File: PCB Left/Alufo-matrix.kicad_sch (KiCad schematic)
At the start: 59 parts, among them K11 PG1350, K12 PG1350, K13 PG1350, K14 PG1350, K15 PG1350, K16 PG1350, K21 PG1350, K22 PG1350, K23 PG1350, K24 PG1350, K25 PG1350, K26 PG1350, K31 PG1350, K32 PG1350, K33 PG1350, K34 PG1350, K35 PG1350, K36 PG1350_1½U

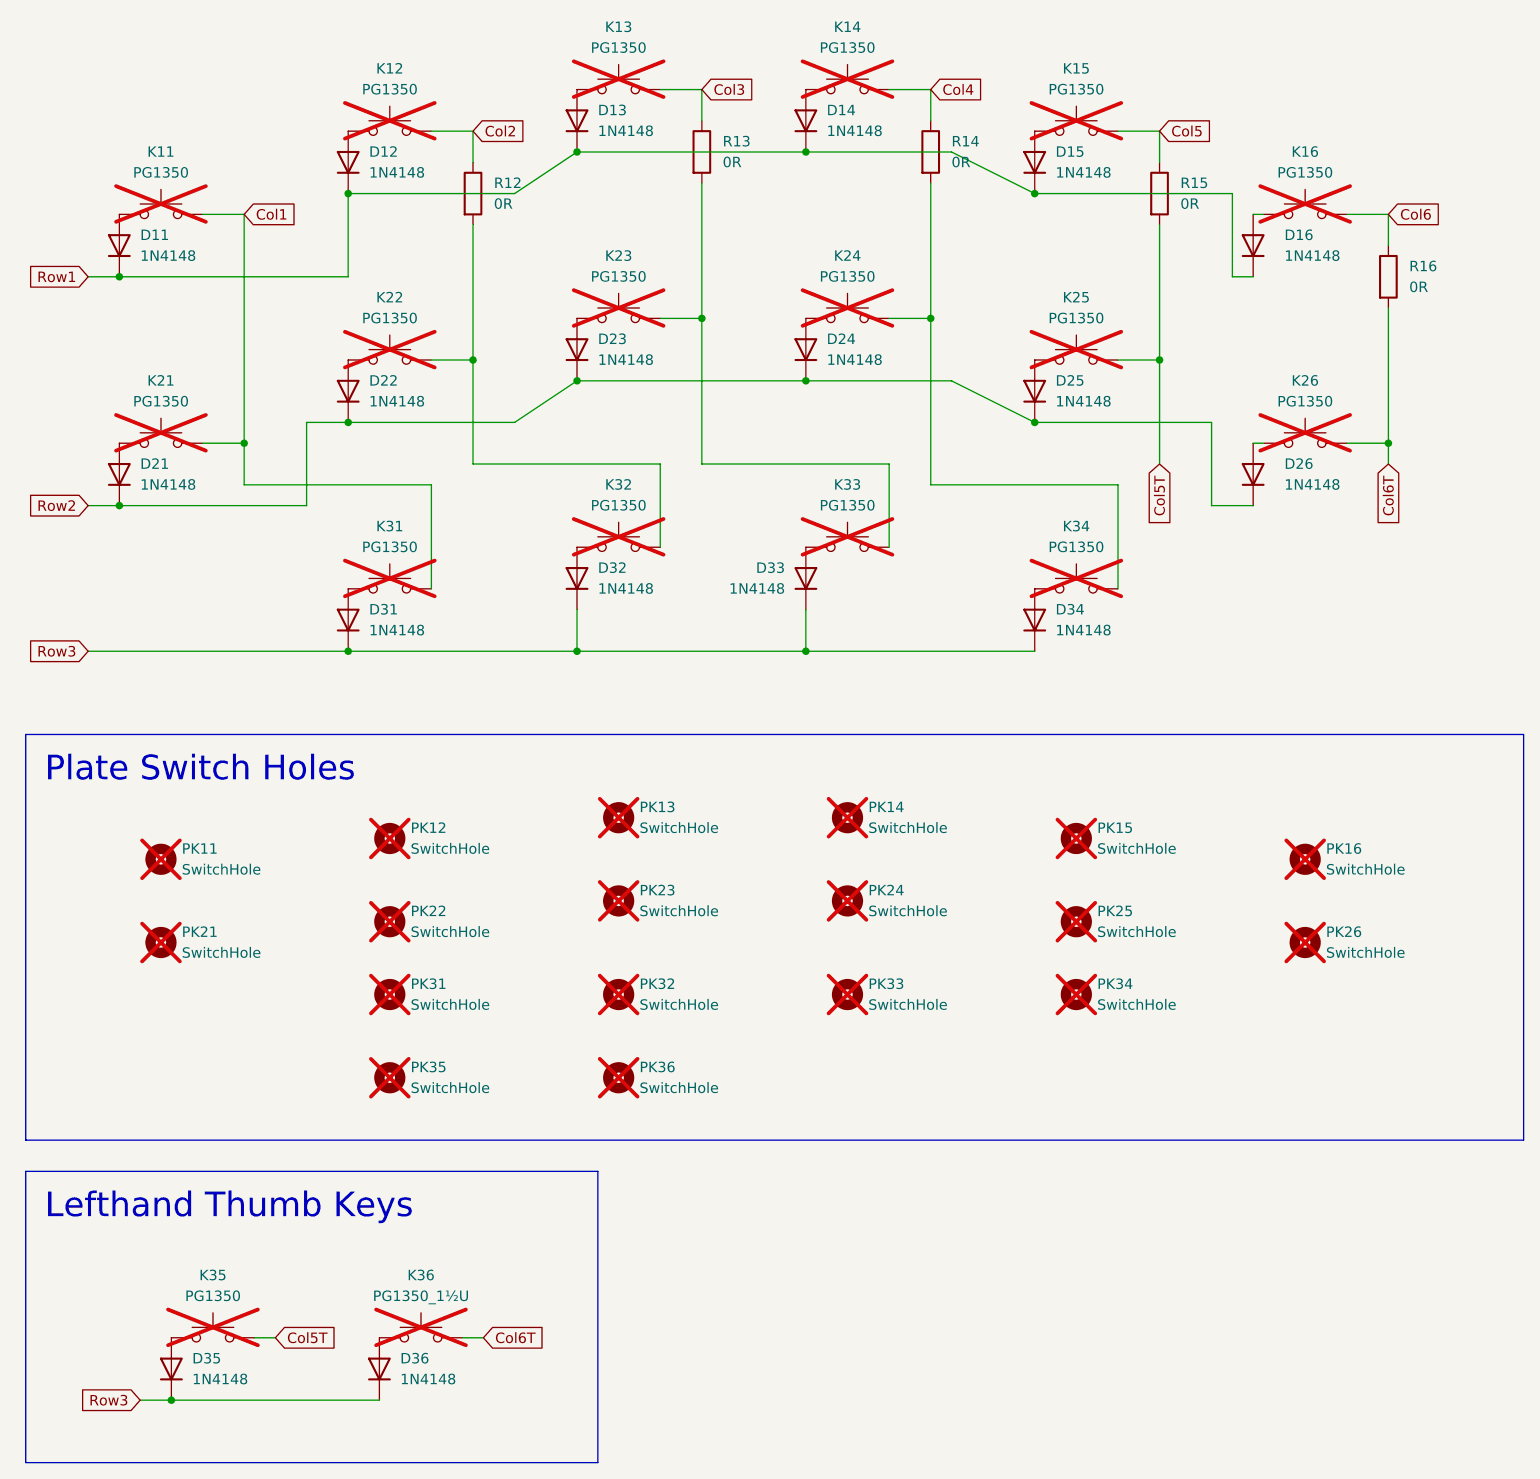
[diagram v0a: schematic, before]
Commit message: Unset DNP on all symbols
It causes the symbol to be obscured by a big red cross in the schematic!
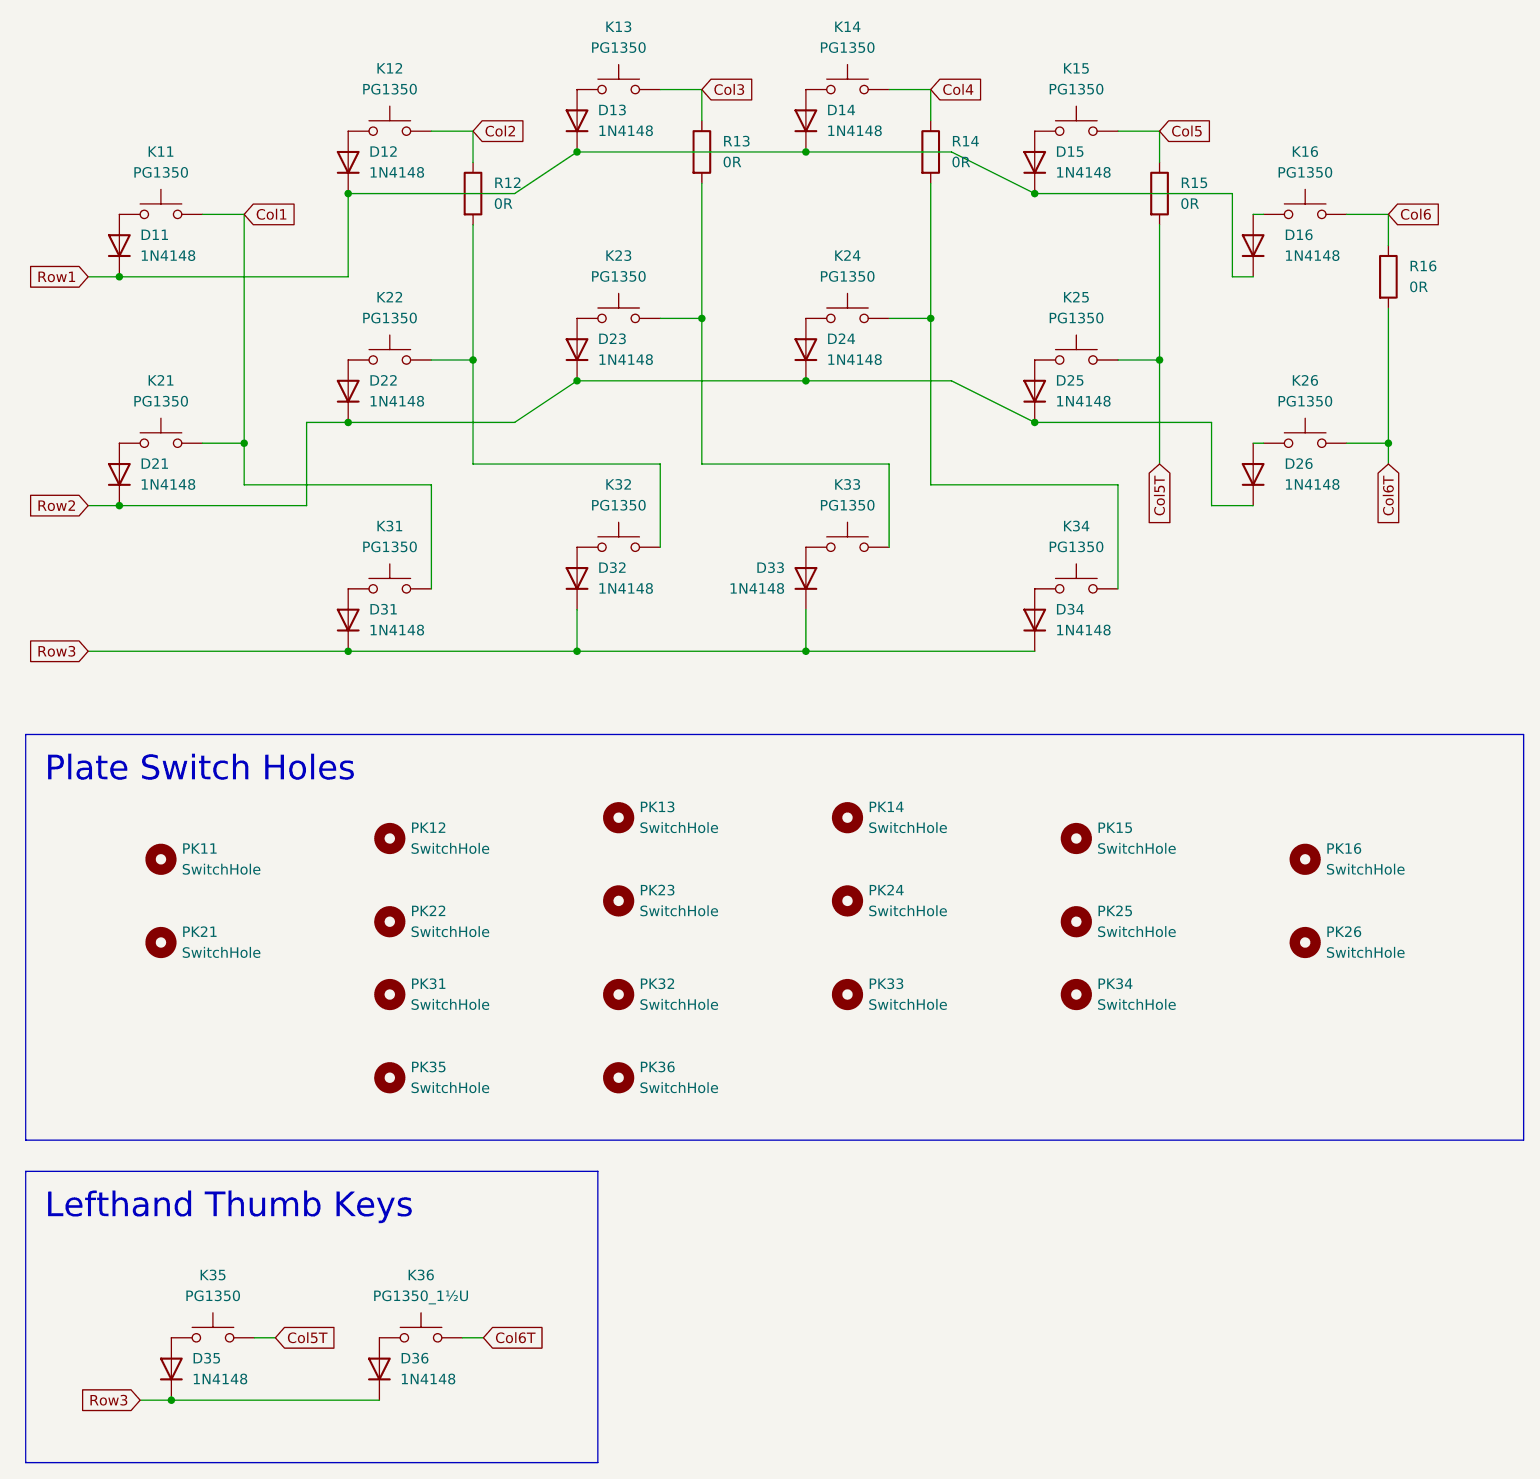
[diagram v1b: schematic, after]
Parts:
- K11, K12, K13, K14, K15, K16, K21, K22, K23, K24, K25, K26, K31, K32, K33, K34, K35, K36, PK11, PK12, PK13, PK14, PK15, PK16, PK21, PK22, PK23, PK24, PK25, PK26, PK31, PK32, PK33, PK34, PK35, PK36: now fitted
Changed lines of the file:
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@@
 		(in_bom no)
 		(on_board yes)
-		(dnp yes)
+		(dnp no)
 		(fields_autoplaced yes)
 		(property "Reference" "PK32"
@@
 		(in_bom no)
 		(on_board yes)
-		(dnp yes)
+		(dnp no)
 		(fields_autoplaced yes)
 		(property "Reference" "PK21"
@@
 		(in_bom yes)
 		(on_board yes)
-		(dnp yes)
+		(dnp no)
 		(property "Reference" "K24"
 			(at 161.29 48.26 0)
@@
 		(in_bom yes)
 		(on_board yes)
-		(dnp yes)
+		(dnp no)
 		(property "Reference" "K23"
 			(at 133.35 48.26 0)
@@
 		(in_bom no)
 		(on_board yes)
-		(dnp yes)
+		(dnp no)
 		(fields_autoplaced yes)
 		(property "Reference" "PK22"
@@
 		(in_bom yes)
 		(on_board yes)
-		(dnp yes)
+		(dnp no)
 		(property "Reference" "K33"
 			(at 161.29 76.2 0)
@@
 		(in_bom yes)
 		(on_board yes)
-		(dnp yes)
+		(dnp no)
 		(property "Reference" "K14"
 			(at 161.29 20.32 0)
@@
 		(in_bom yes)
 		(on_board yes)
-		(dnp yes)
+		(dnp no)
 		(property "Reference" "K34"
 			(at 189.23 81.28 0)
@@
 		(in_bom no)
 		(on_board yes)
-		(dnp yes)
+		(dnp no)
 		(fields_autoplaced yes)
 		(property "Reference" "PK15"
@@
 		(in_bom yes)
 		(on_board yes)
-		(dnp yes)
+		(dnp no)
 		(property "Reference" "K36"
 			(at 109.22 172.72 0)
@@
 		(in_bom yes)
 		(on_board yes)
-		(dnp yes)
+		(dnp no)
 		(property "Reference" "K11"
 			(at 77.47 35.56 0)
@@
 		(in_bom no)
 		(on_board yes)
-		(dnp yes)
+		(dnp no)
 		(fields_autoplaced yes)
 		(property "Reference" "PK14"
@@
 		(in_bom no)
 		(on_board yes)
-		(dnp yes)
+		(dnp no)
 		(fields_autoplaced yes)
 		(property "Reference" "PK13"
@@
 		(in_bom yes)
 		(on_board yes)
-		(dnp yes)
+		(dnp no)
 		(property "Reference" "K31"
 			(at 105.41 81.28 0)
@@
 		(in_bom yes)
 		(on_board yes)
-		(dnp yes)
+		(dnp no)
 		(property "Reference" "K21"
 			(at 77.47 63.5 0)
@@
 		(in_bom yes)
 		(on_board yes)
-		(dnp yes)
+		(dnp no)
 		(property "Reference" "K15"
 			(at 189.23 25.4 0)
@@
 		(in_bom yes)
 		(on_board yes)
-		(dnp yes)
+		(dnp no)
 		(property "Reference" "K32"
 			(at 133.35 76.2 0)
@@
 		(in_bom yes)
 		(on_board yes)
-		(dnp yes)
+		(dnp no)
 		(property "Reference" "K12"
 			(at 105.41 25.4 0)
@@
 		(in_bom yes)
 		(on_board yes)
-		(dnp yes)
+		(dnp no)
 		(property "Reference" "K35"
 			(at 83.82 172.72 0)
@@
 		(in_bom yes)
 		(on_board yes)
-		(dnp yes)
+		(dnp no)
 		(property "Reference" "K25"
 			(at 189.23 53.34 0)
@@
 		(in_bom no)
 		(on_board yes)
-		(dnp yes)
+		(dnp no)
 		(fields_autoplaced yes)
 		(property "Reference" "PK33"
@@
 		(in_bom no)
 		(on_board yes)
-		(dnp yes)
+		(dnp no)
 		(fields_autoplaced yes)
 		(property "Reference" "PK12"
@@
 		(in_bom no)
 		(on_board yes)
-		(dnp yes)
+		(dnp no)
 		(fields_autoplaced yes)
 		(property "Reference" "PK23"
@@
 		(in_bom no)
 		(on_board yes)
-		(dnp yes)
+		(dnp no)
 		(fields_autoplaced yes)
 		(property "Reference" "PK25"
@@
 		(in_bom no)
 		(on_board yes)
-		(dnp yes)
+		(dnp no)
 		(fields_autoplaced yes)
 		(property "Reference" "PK34"
@@
 		(in_bom no)
 		(on_board yes)
-		(dnp yes)
+		(dnp no)
 		(fields_autoplaced yes)
 		(property "Reference" "PK26"
@@
 		(in_bom no)
 		(on_board yes)
-		(dnp yes)
+		(dnp no)
 		(fields_autoplaced yes)
 		(property "Reference" "PK36"
@@
 		(in_bom no)
 		(on_board yes)
-		(dnp yes)
+		(dnp no)
 		(fields_autoplaced yes)
 		(property "Reference" "PK31"
@@
 		(in_bom no)
 		(on_board yes)
-		(dnp yes)
+		(dnp no)
 		(fields_autoplaced yes)
 		(property "Reference" "PK24"
@@
 		(in_bom yes)
 		(on_board yes)
-		(dnp yes)
+		(dnp no)
 		(property "Reference" "K22"
 			(at 105.41 53.34 0)
@@
 		(in_bom no)
 		(on_board yes)
-		(dnp yes)
+		(dnp no)
 		(fields_autoplaced yes)
 		(property "Reference" "PK35"
@@
 		(in_bom yes)
 		(on_board yes)
-		(dnp yes)
+		(dnp no)
 		(property "Reference" "K13"
 			(at 133.35 20.32 0)
@@
 		(in_bom no)
 		(on_board yes)
-		(dnp yes)
+		(dnp no)
 		(fields_autoplaced yes)
 		(property "Reference" "PK16"
@@
 		(in_bom yes)
 		(on_board yes)
-		(dnp yes)
+		(dnp no)
 		(property "Reference" "K26"
 			(at 217.17 63.5 0)
@@
 		(in_bom no)
 		(on_board yes)
-		(dnp yes)
+		(dnp no)
 		(fields_autoplaced yes)
 		(property "Reference" "PK11"
@@
 		(in_bom yes)
 		(on_board yes)
-		(dnp yes)
+		(dnp no)
 		(property "Reference" "K16"
 			(at 217.17 35.56 0)

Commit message: Remove one-sided board workarounds
The v2 board will be a regular two-layer FR4 board. The aluminium board was two hard to solder without shorts developing. A two-layer board does not need the 0Ω jumper resistors as we can flip just go to the other layer with vias.
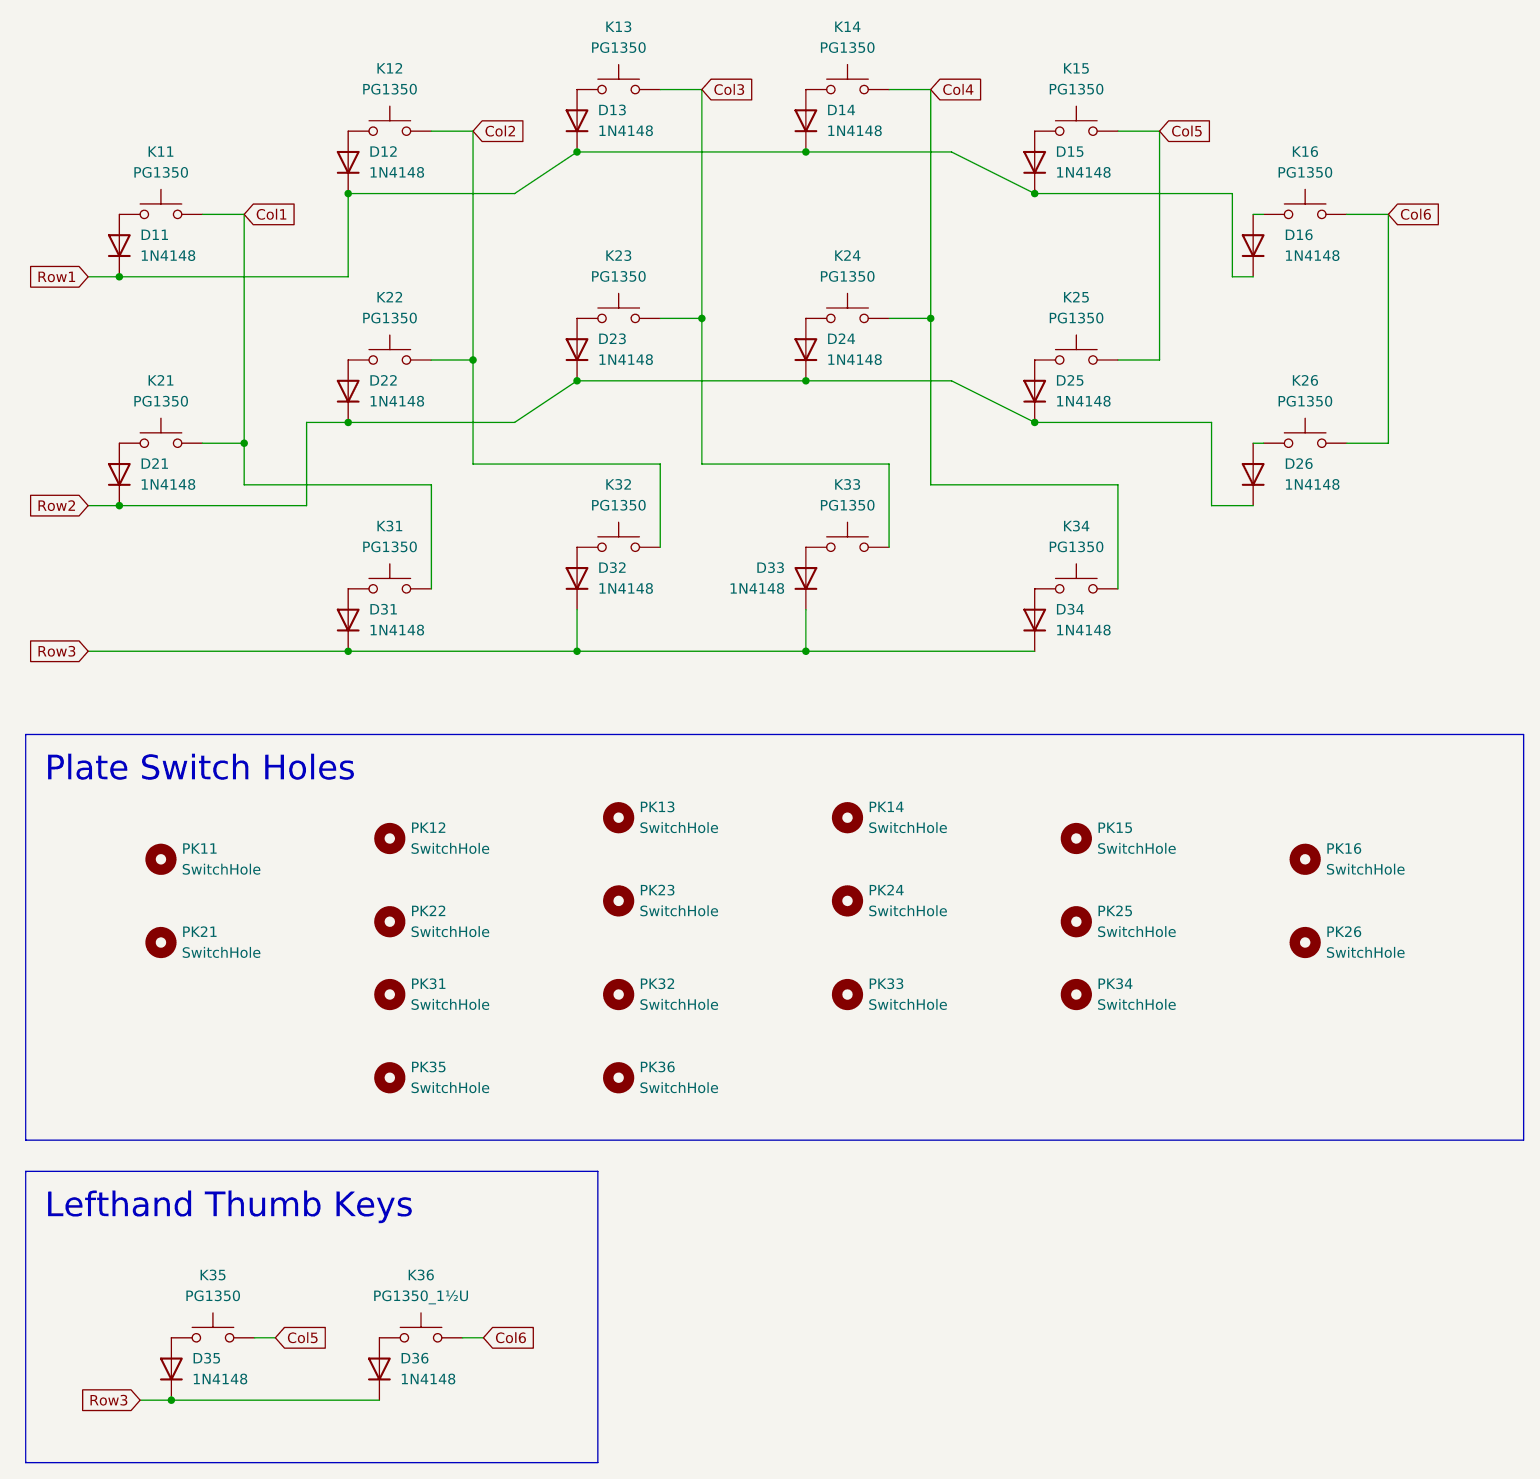
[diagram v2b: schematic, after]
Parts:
- removed R12, R13, R14, R15, R16: 0R, Resistor_SMD:R_2010_5025Metric, symbol Device:R
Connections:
- net Col5T is gone; now on net Col5: K25.1, K35.1
- net Col6T is gone; now on net Col6: K26.1, K36.1
- net Col2: now also K22.1, K32.1
- net Col3: now also K23.1, K33.1
- net Col4: now also K24.1, K34.1
